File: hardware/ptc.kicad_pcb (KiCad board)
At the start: 2 copper layers, 35 x 30 mm, 37 parts, among them J1 AKL_5_2, J2 AKL_5_2, P1 CON-SENSOR, P2 Debug, P3 Boot, P4 CONN_02X04, P5 CONN_02X04, U1 XMC1XXX24, U2 MAX31865, U3 DRILL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

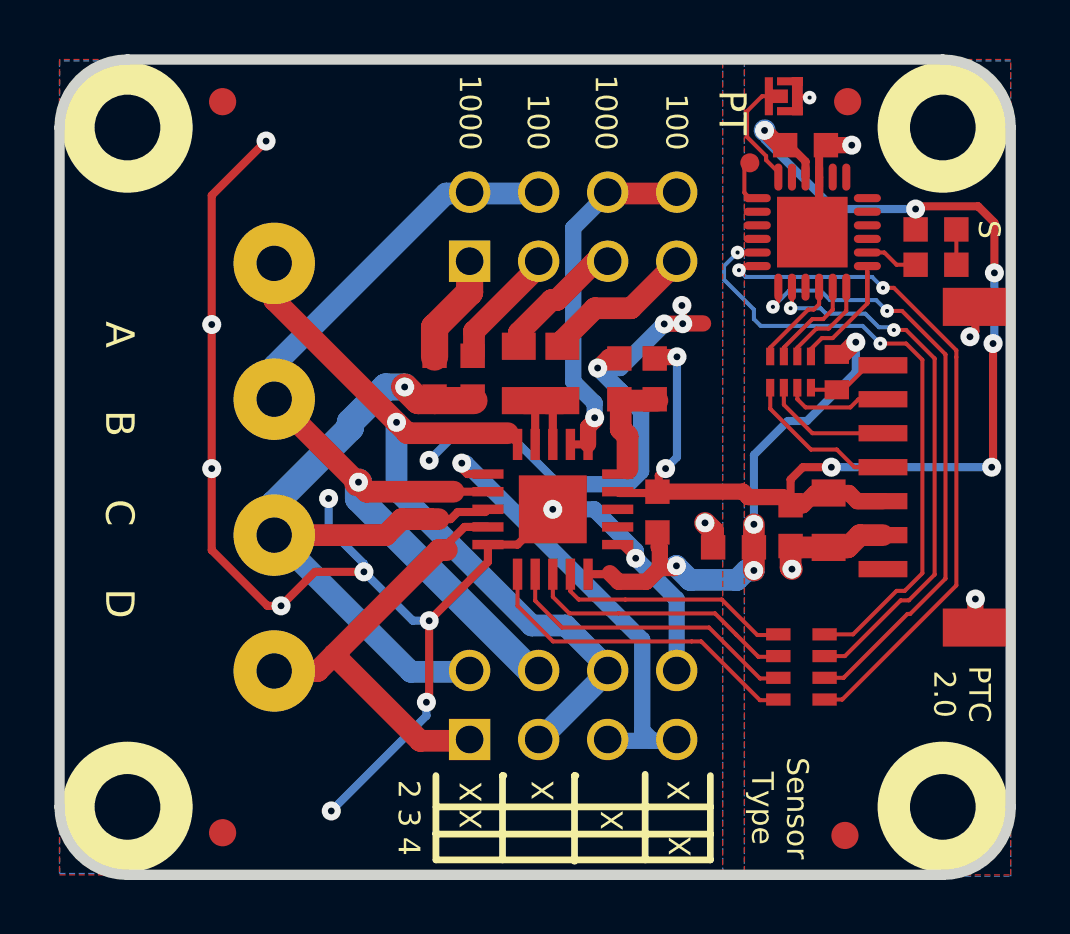
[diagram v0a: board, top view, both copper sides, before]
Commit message: change default via size
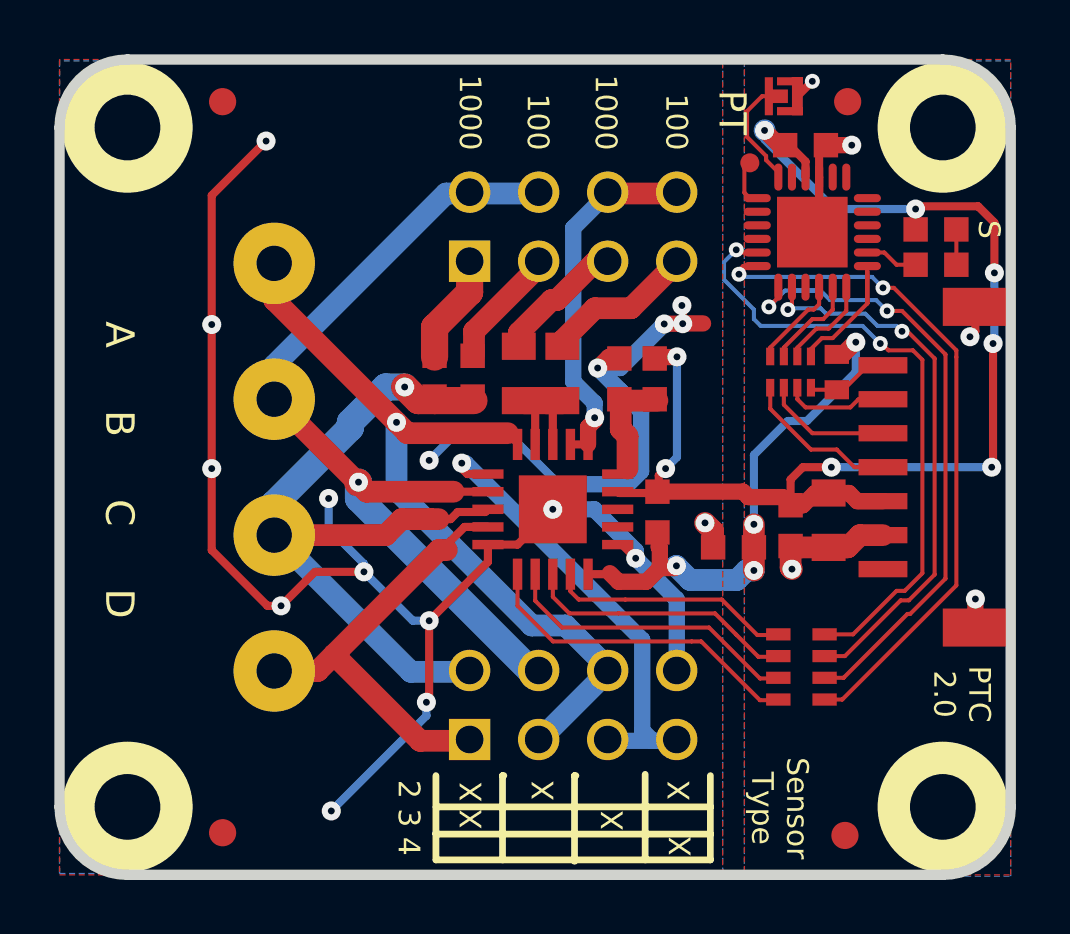
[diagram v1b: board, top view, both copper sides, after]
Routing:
- net M-MOSI: track 25.2 -> 30.9 mm
- net M-CLK: track 22.6 -> 24.0 mm
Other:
- net class Default: via_dia 0.70104 -> 0.7; via_drill 0.24892 -> 0.25
- rule via_min_drill: 0.15 -> 0.25
- rule via_min_size: 0.5 -> 0.55

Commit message: fix description text
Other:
- board text added: "Pt"
- board text removed: "PT"
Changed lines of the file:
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@@
   )
   (layers
-    (0 Vorderseite signal)
-    (31 Rückseite signal)
+    (0 Vorderseite signal hide)
+    (31 Rückseite signal hide)
     (32 B.Adhes user)
     (33 F.Adhes user hide)
@@
   )
   (setup
-    (last_trace_width 0.15)
+    (last_trace_width 0.29972)
     (user_trace_width 0.15)
     (user_trace_width 0.29972)
@@
     (aux_axis_origin 159.9 99.95)
     (grid_origin 159.9 99.95)
-    (visible_elements FFFFFFBF)
+    (visible_elements FFFF7FBF)
     (pcbplotparams
       (layerselection 0x00030_80000001)
@@
     (effects (font (size 0.8001 0.8001) (thickness 0.14986)))
   )
-  (gr_text PT (at 149.64918 71.89978 270) (layer F.SilkS)
+  (gr_text Pt (at 149.64918 71.89978 270) (layer F.SilkS)
     (effects (font (size 1.00076 1.00076) (thickness 0.20066)))
   )

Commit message: specify processor
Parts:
- U1: value XMC1XXX24 -> XMC1100
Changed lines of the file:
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@@
       (effects (font (size 0.3 0.3) (thickness 0.075)))
     )
-    (fp_text value XMC1XXX24 (at 0 0.8 180) (layer F.Fab)
+    (fp_text value XMC1100 (at 0 0.8 180) (layer F.Fab)
       (effects (font (size 0.3 0.3) (thickness 0.075)))
     )
